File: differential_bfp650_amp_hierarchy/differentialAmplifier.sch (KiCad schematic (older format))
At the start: 26 parts, among them U1 BFP650, U2 BFP650, U3 BFP650, U4 BFP650, U5 BFP650, U6 BFP650

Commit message: Tuned simulation. Added extra RC in collector of differential amplifier output buffer. Tuned values to restore stability
Simulating 10 SiPM in parallel by increasing number of pixels x10 w.r.t.
model of single 3x3mm^2 SiPM

Peaking time ~ 800ns
Gain ~ 1 mV per Pixel Avalanche.
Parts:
- added C15, C16: 10u, symbol Device:C
- added R51, R52: 50, symbol Device:R
- C3: value C -> 10u
- R1, R16: value 1K -> 100; Spice_Model 1K -> 100
- R17, R2: value 4k -> 8k; Spice_Model 4k -> 8k
- R9: value 1k -> 500
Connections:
- net 0: now also C15.2, C16.2
- net vcoutm: now also R51.2; no longer R1.2
- net vcoutp: now also R52.2; no longer R16.2
- new net: C16.1, R16.2, R52.1
- new net: C15.1, R1.2, R51.1
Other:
- note added: "+4.4V\n"
- note added: "-1.78V\n"
- note added: "Bias Vin+/- to approx -1.5V. \nBias current approx 7.5uA"
- note removed: "+PSPICE \n* .control\n* ac dec 66 1kHz 120kHz \n* plot vdb(/voutp)\n* set units = degrees\n* plot vp(“/voutp”)\n* .endc"
- note removed: "Bias Vin+/- to approx -1.5V. \nBias current approx 75uA"
- moved on the sheet: R28, R41

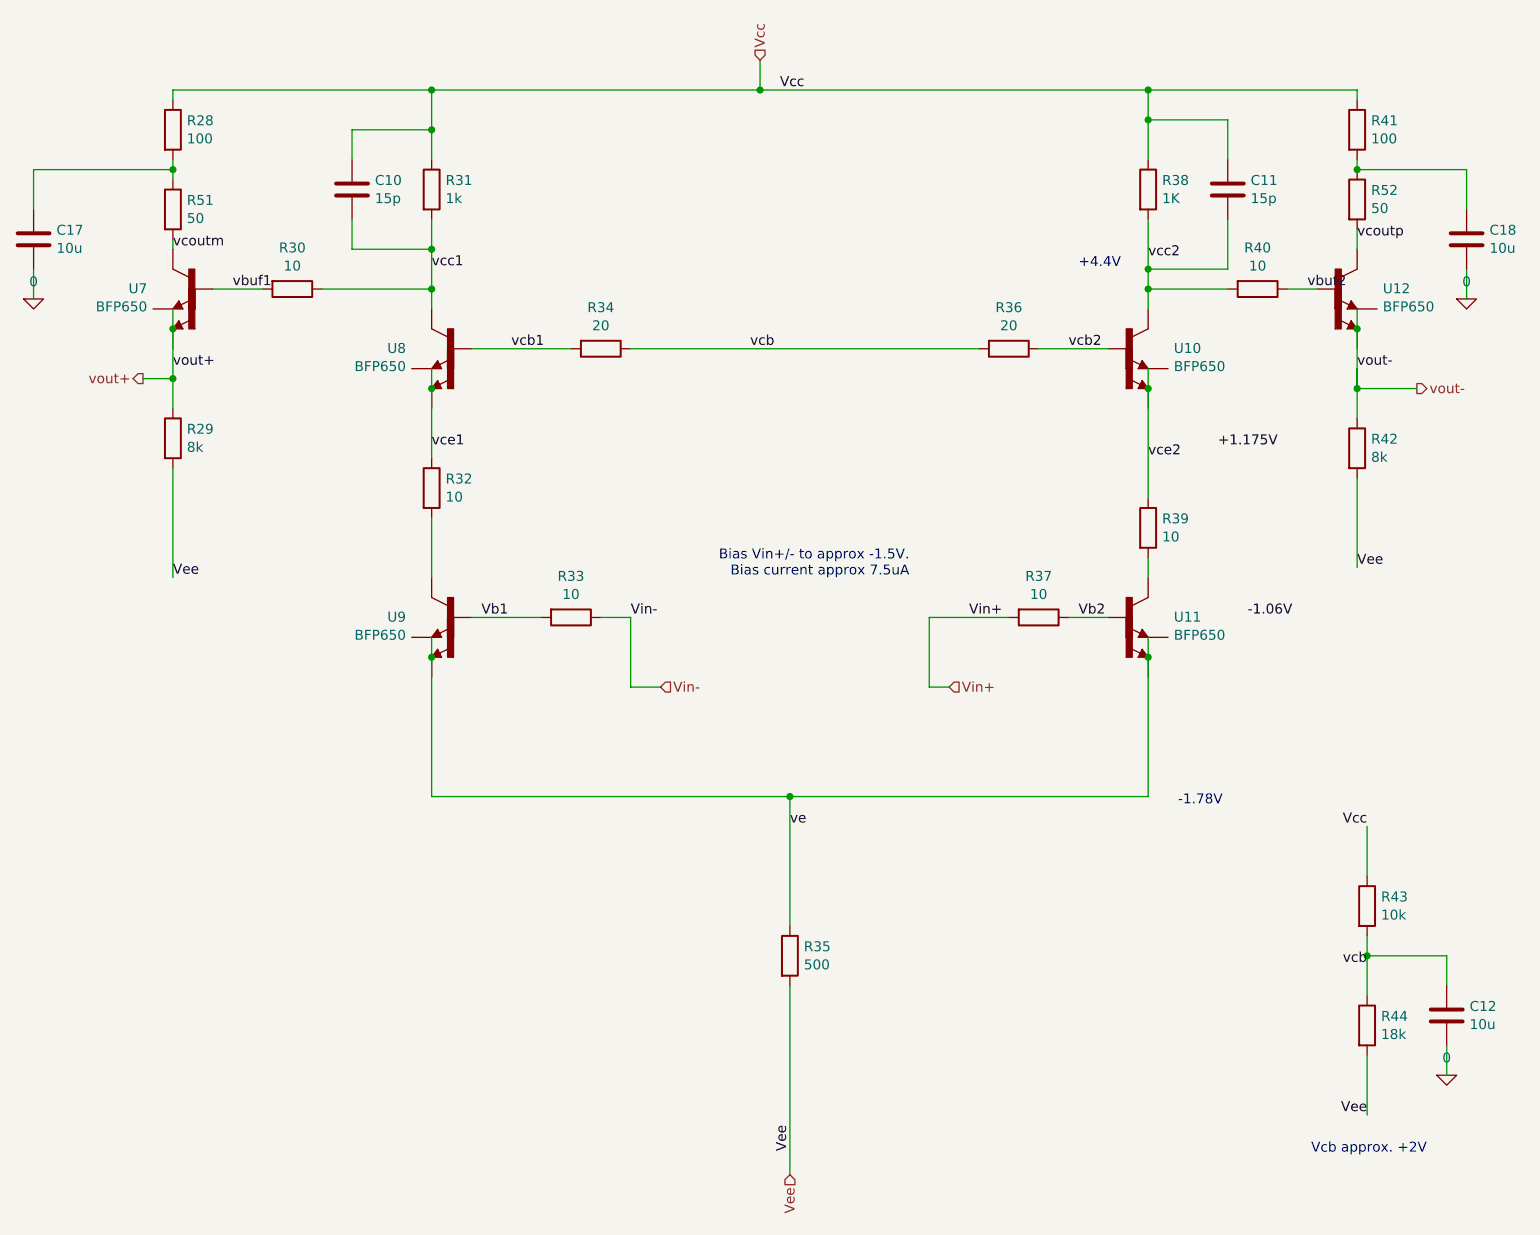
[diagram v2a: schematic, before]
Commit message: More hacking to get circuit stable at -186 degC ( still slight ringing )
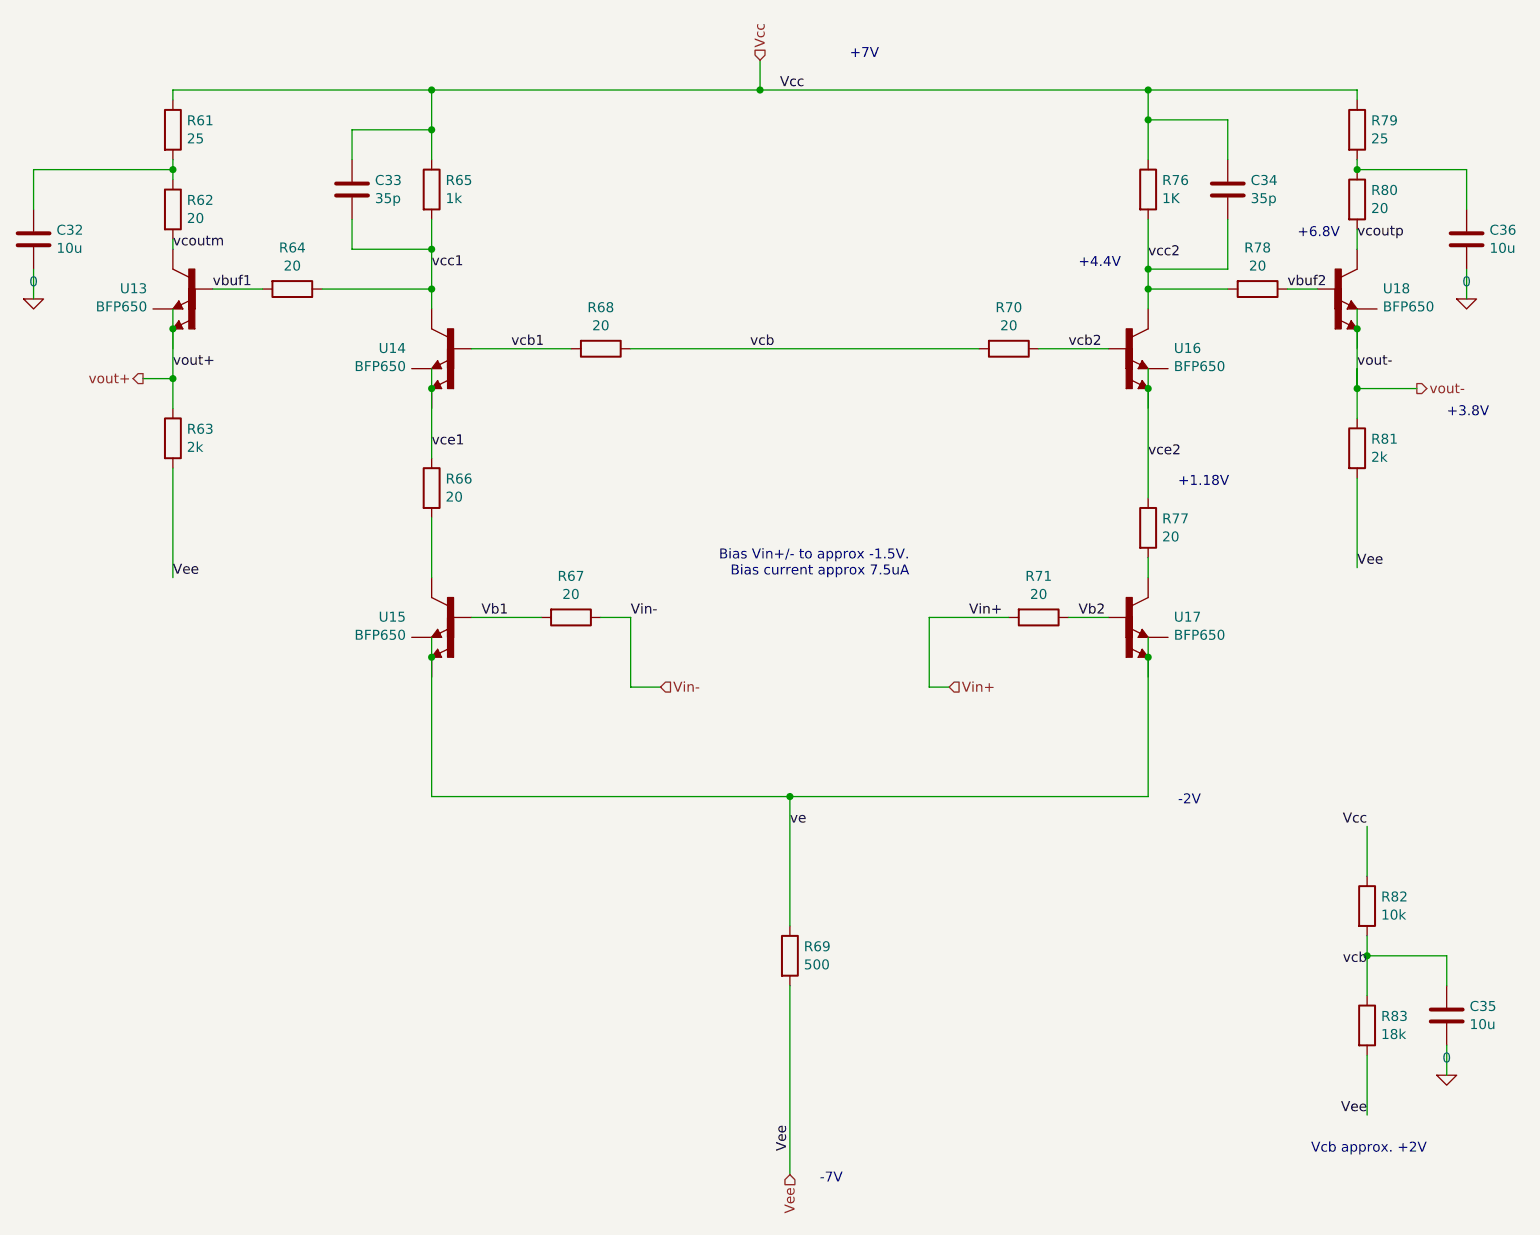
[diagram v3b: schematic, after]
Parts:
- C1, C2: value 15p -> 35p; Spice_Model 15p -> 35p
- R1, R16: value 100 -> 25; Spice_Model 100 -> 25
- R11, R7: value 10 -> 20
- R13, R15, R3, R5: value 10 -> 20; Spice_Model 10 -> 20
- R17, R2: value 8k -> 2k; Spice_Model 8k -> 2k
- R51, R52: value 50 -> 20
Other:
- note added: "+1.18V"
- note added: "+3.8V\n"
- note added: "+6.8V"
- note added: "+7V\n"
- note added: "-2V\n"
- note added: "-7V"
- note removed: "-1.78V\n"
